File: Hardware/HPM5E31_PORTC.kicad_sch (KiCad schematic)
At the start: 1 part, among them U1 HPM5E31IGN1

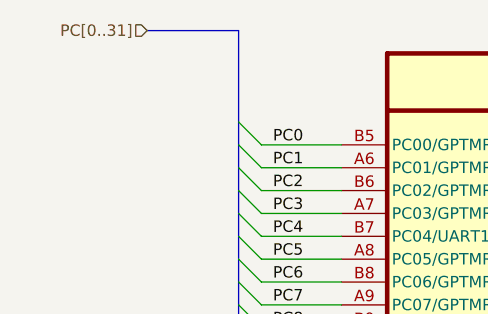
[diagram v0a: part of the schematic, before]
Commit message: 新增ESC IO引出，ESC CTR LED，EUI接口
编码器接口电源输出加保险，SPI加ESD
PY32ADC外部接口加ESD
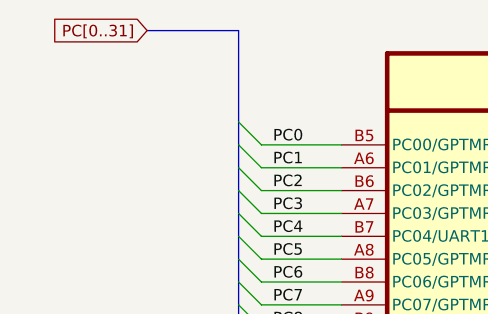
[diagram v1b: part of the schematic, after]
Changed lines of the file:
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@@
 		)
 	)
-	(hierarchical_label "PC[0..31]"
+	(global_label "PC[0..31]"
 		(shape input)
 		(at 40.64 41.91 180)
+		(fields_autoplaced yes)
 		(effects
 			(font
@@
 			(justify right)
 		)
+		(property "Intersheetrefs" "${INTERSHEET_REFS}"
+			(at 28.5833 41.91 0)
+			(effects
+				(font
+					(size 1.27 1.27)
+				)
+				(justify right)
+				(hide yes)
+			)
+		)
 	)

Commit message: 拉线
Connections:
- net PC0: no longer U1.B5 (PC00/GPTMR1.COMP0/UART0.TXD/MCAN0.TXD/ESC0.GPI63/ESC0.GPO00/PPI0.DQ24/XPI0.CB_CS0/PWM0.P0/TRGM.P00/ESC0.GPI15/OWR0.DAT)
- net PC1: no longer U1.A6 (PC01/GPTMR1.CAPT0/UART0.RXD/MCAN0.RXD/ESC0.GPI62/ESC0.GPO01/PPI0.DQ25/XPI0.CB_D1/PWM0.P1/TRGM.P01/ESC0.GPI14/OWR1.DAT)
- net PC10: no longer U1.D5 (PC10/GPTMR0.COMP2/UART2.DE/UART2.RTS/SPI1.SCLK/MCAN2.STBY/ESC0.GPI53/ESC0.GPO10/PPI0.DQ20/XPI0.CB_D0/PWM1.P2/TRGM.P10/ESC0.GPI05/QEI1.F/ESC0.CTR1)
- net PC11: no longer U1.C6 (PC11/UART2.CTS/SPI1.CS0/ESC0.GPI52/ESC0.GPO11/PPI0.DQ21/XPI0.CB_DQS/PWM1.P3/TRGM.P11/ESC0.GPI04/QEI1.H0/ESC0.CTR2)
- net PC12: no longer U1.D6 (PC12/UART3.CTS/I2C1.SDA/SPI1.MISO/ESC0.GPI51/ESC0.GPO12/PPI0.DM2/XPI0.CA_D2/PWM1.P4/TRGM.P12/ESC0.GPI03/QEI1.Z/QEO1.Z/ESC0.CTR3)
- net PC13: no longer U1.C7 (PC13/GPTMR1.COMP3/UART3.DE/UART3.RTS/I2C1.SCL/SPI1.MOSI/MCAN3.STBY/ESC0.GPI50/ESC0.GPO13/PPI0.DQ18/XPI0.CA_CS1/PWM1.P5/TRGM.P13/ESC0.GPI02/QEI1.A/QEO1.A/ESC0.CTR4)
- net PC14: no longer U1.D7 (PC14/UART3.RXD/SPI1.DAT2/MCAN3.RXD/ESC0.GPI49/ESC0.GPO14/PPI0.DQ19/PWM1.P6/TRGM.P14/ESC0.GPI01/QEI1.B/QEO1.B/ESC0.CTR5)
- net PC15: now also U1.J9 (VANA); no longer U1.C8 (PC15/GPTMR0.COMP3/UART3.TXD/SPI1.DAT3/MCAN3.TXD/ESC0.GPI48/ESC0.GPO15/PPI0.DM3/XPI0.CA_D0/PWM1.P7/TRGM.P15/ESC0.GPI00/ESC0.CTR6)
- net PC16: no longer U1.D8 (PC16/GPTMR3.COMP0/UART4.TXD/ESC0.GPI47/ESC0.GPO16/PPI0.DQ16/XPI0.CA_DQS/ESC0.CTR7)
- net PC17: no longer U1.C9 (PC17/GPTMR3.CAPT0/UART4.RXD/ESC0.GPI46/ESC0.GPO17/PPI0.DQ17/ESC0.CTR8)
- net PC18: now also U1.H8 (VSSA); no longer U1.A10 (PC18/GPTMR3.COMP1/UART4.DE/UART4.RTS/ESC0.GPI45/ESC0.GPO18/PPI0.DQ04/ESC0.CTR0)
- net PC19: no longer U1.B10 (PC19/GPTMR3.CAPT1/UART4.CTS/SPI2.CS3/ESC0.GPI44/ESC0.GPO19/PPI0.DQ05/ESC0.CTR1)
- net PC2: no longer U1.B6 (PC02/GPTMR1.COMP1/UART0.DE/UART0.RTS/I2C2.SCL/MCAN0.STBY/ESC0.GPI61/ESC0.GPO02/PPI0.DQ22/XPI0.CB_D2/PWM0.P2/TRGM.P02/ESC0.GPI13/QEI0.H1)
- net PC20: no longer U1.A11 (PC20/UART5.CTS/SPI3.SCLK/ESC0.GPI43/ESC0.GPO20/PPI0.DQ06/ESC0.CTR2)
- net PC21: no longer U1.B11 (PC21/GPTMR3.COMP2/UART5.DE/UART5.RTS/SPI3.CS0/ESC0.GPI42/ESC0.GPO21/PPI0.DQ07/ESC0.CTR3/QEO1.Z)
- net PC22: no longer U1.A12 (PC22/GPTMR2.CAPT0/UART5.RXD/SPI3.MISO/ESC0.GPI41/ESC0.GPO22/PPI0.CTR2/QEO1.B)
- net PC23: no longer U1.A13 (PC23/GPTMR2.COMP0/UART5.TXD/SPI3.MOSI/ESC0.GPI40/ESC0.GPO23/PPI0.DQ08/QEO1.A)
- net PC24: no longer U1.B14 (PC24/GPTMR2.COMP1/UART6.TXD/SPI2.CS2/ESC0.GPI39/ESC0.GPO24/PPI0.DQ09)
- net PC25: no longer U1.C14 (PC25/GPTMR2.CAPT1/UART6.RXD/SPI2.CS1/ESC0.GPI38/ESC0.GPO25/PPI0.DQ11)
- net PC26: no longer U1.D14 (PC26/GPTMR2.COMP2/UART6.DE/UART6.RTS/SPI2.SCLK/ESC0.GPI37/ESC0.GPO26/PPI0.DQ12/QEI1.H1)
- net PC27: no longer U1.D13 (PC27/UART6.CTS/SPI2.CS0/ESC0.GPI36/ESC0.GPO27/PPI0.CTR0/ESC0.CTR4/QEI1.F)
- net PC28: no longer U1.E14 (PC28/UART7.CTS/SPI2.MISO/ESC0.GPI35/ESC0.GPO28/PPI0.DM0/ESC0.CTR5/QEI1.H0)
- net PC29: no longer U1.E13 (PC29/GPTMR3.COMP3/UART7.DE/UART7.RTS/SPI2.MOSI/ESC0.GPI34/ESC0.GPO29/PPI0.CLK/ESC0.CTR6/QEI1.Z/SOC.REF0)
- net PC3: no longer U1.A7 (PC03/GPTMR1.CAPT1/UART0.CTS/I2C2.SDA/SPI1.CS3/MCAN1.STBY/ESC0.GPI60/ESC0.GPO03/PPI0.DQ26/XPI0.CB_D3/PWM0.P3/TRGM.P03/ESC0.GPI12/QEI0.F)
- net PC30: no longer U1.F14 (PC30/UART7.RXD/SPI2.DAT2/ESC0.GPI33/ESC0.GPO30/PPI0.CS0/ESC0.CTR7/QEI1.A/SOC.REF1)
- net PC31: no longer U1.F13 (PC31/GPTMR2.COMP3/UART7.TXD/SPI2.DAT3/ESC0.GPI32/ESC0.GPO31/PPI0.CS1/ESC0.CTR8/QEI1.B)
- net PC4: no longer U1.B7 (PC04/UART1.CTS/SPI0.SCLK/MCAN1.RXD/ESC0.GPI59/ESC0.GPO04/PPI0.DQ27/XPI0.CB_SCLK/PWM0.P4/TRGM.P04/ESC0.GPI11/QEI0.H0)
- net PC5: no longer U1.A8 (PC05/GPTMR1.COMP2/UART1.DE/UART1.RTS/SPI0.CS0/MCAN1.TXD/ESC0.GPI58/ESC0.GPO05/PPI0.DQ28/XPI0.CA_CS0/PWM0.P5/TRGM.P05/ESC0.GPI10/QEI0.Z/QEO0.Z)
- net PC6: no longer U1.B8 (PC06/GPTMR0.CAPT0/UART1.RXD/I2C3.SDA/SPI0.MISO/ESC0.GPI57/ESC0.GPO06/PPI0.DQ29/XPI0.CA_D1/PWM0.P6/TRGM.P06/ESC0.GPI09/QEI0.B/QEO0.B)
- net PC7: now also U1.N1 (DCDC_GND); no longer U1.A9 (PC07/GPTMR0.COMP0/UART1.TXD/I2C3.SCL/SPI0.MOSI/ESC0.GPI56/ESC0.GPO07/PPI0.DQ30/XPI0.CA_D3/PWM0.P7/TRGM.P07/ESC0.GPI08/QEI0.A/QEO0.A)
- net PC8: now also U1.P2 (DCDC_GND); no longer U1.B9 (PC08/GPTMR0.COMP1/UART2.TXD/I2C0.SCL/SPI1.CS2/MCAN2.TXD/ESC0.GPI55/ESC0.GPO08/PPI0.DQ31/XPI0.CA_SCLK/PWM1.P0/TRGM.P08/ESC0.GPI07)
- net PC9: no longer U1.C5 (PC09/GPTMR0.CAPT1/UART2.RXD/I2C0.SDA/SPI1.CS1/MCAN2.RXD/ESC0.GPI54/ESC0.GPO09/PPI0.DQ23/XPI0.CB_CS1/PWM1.P1/TRGM.P09/ESC0.GPI06/QEI1.H1/ESC0.CTR0)
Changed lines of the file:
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@@
+		)
+	)
+	(label "PC30"
+		(at 54.61 130.81 0)
+		(effects
+			(font
+				(size 1.27 1.27)
+			)
+			(justify left bottom)
+		)
+	)
+	(label "PC27"
+		(at 54.61 123.19 0)
+		(effects
+			(font
+				(size 1.27 1.27)
+			)
+			(justify left bottom)
+		)
+	)
+	(label "PC20"
+		(at 54.61 105.41 0)
+		(effects
+			(font
+				(size 1.27 1.27)
+			)
+			(justify left bottom)
+		)
+	)
+	(label "PC4"
+		(at 54.61 64.77 0)
+		(effects
+			(font
+				(size 1.27 1.27)
+			)
+			(justify left bottom)
+		)
+	)
+	(label "PC16"
+		(at 54.61 95.25 0)
+		(effects
+			(font
+				(size 1.27 1.27)
+			)
+			(justify left bottom)
+		)
+	)
+	(label "PC15"
+		(at 54.61 92.71 0)
+		(effects
+			(font
+				(size 1.27 1.27)
+			)
+			(justify left bottom)
+		)
+	)
+	(label "PC12"
+		(at 54.61 85.09 0)
+		(effects
+			(font
+				(size 1.27 1.27)
+			)
+			(justify left bottom)
+		)
+	)
+	(label "PC6"
+		(at 54.61 69.85 0)
+		(effects
+			(font
+				(size 1.27 1.27)
+			)
+			(justify left bottom)
+		)
+	)
+	(label "PC31"
+		(at 54.61 133.35 0)
+		(effects
+			(font
+				(size 1.27 1.27)
+			)
+			(justify left bottom)
+		)
+	)
+	(label "PC18"
+		(at 54.61 100.33 0)
+		(effects
+			(font
+				(size 1.27 1.27)
+			)
+			(justify left bottom)
+		)
+	)
+	(label "PC14"
+		(at 54.61 90.17 0)
+		(effects
+			(font
+				(size 1.27 1.27)
+			)
+			(justify left bottom)
+		)
+	)
+	(label "PC0"
+		(at 54.61 54.61 0)
+		(effects
+			(font
+				(size 1.27 1.27)
+			)
+			(justify left bottom)
+		)
+	)
+	(label "PC7"
+		(at 54.61 72.39 0)
+		(effects
+			(font
+				(size 1.27 1.27)
+			)
+			(justify left bottom)
+		)
+	)
+	(label "PC17"
+		(at 54.61 97.79 0)
+		(effects
+			(font
+				(size 1.27 1.27)
+			)
+			(justify left bottom)
+		)
+	)
+	(label "PC5"
+		(at 54.61 67.31 0)
+		(effects
+			(font
+				(size 1.27 1.27)
+			)
+			(justify left bottom)
+		)
+	)
+	(label "PC13"
+		(at 54.61 87.63 0)
+		(effects
+			(font
+				(size 1.27 1.27)
+			)
+			(justify left bottom)
+		)
+	)
+	(label "PC2"
+		(at 54.61 59.69 0)
+		(effects
+			(font
+				(size 1.27 1.27)
+			)
+			(justify left bottom)
+		)
+	)
+	(label "PC29"
+		(at 54.61 128.27 0)
+		(effects
+			(font
+				(size 1.27 1.27)
+			)
+			(justify left bottom)
+		)
+	)
+	(label "PC23"
+		(at 54.61 113.03 0)
+		(effects
+			(font
+				(size 1.27 1.27)
+			)
+			(justify left bottom)
 		)
 	)
 	(label "PC10"
 		(at 54.61 80.01 0)
-		(effects
-			(font
-				(size 1.27 1.27)
-			)
-			(justify left bottom)
-		)
-	)
-	(label "PC30"
-		(at 54.61 130.81 0)
-		(effects
-			(font
-				(size 1.27 1.27)
-			)
-			(justify left bottom)
-		)
-	)
-	(label "PC27"
-		(at 54.61 123.19 0)
-		(effects
-			(font
-				(size 1.27 1.27)
-			)
-			(justify left bottom)
-		)
-	)
-	(label "PC20"
-		(at 54.61 105.41 0)
-		(effects
-			(font
-				(size 1.27 1.27)
-			)
-			(justify left bottom)
-		)
-	)
-	(label "PC4"
-		(at 54.61 64.77 0)
-		(effects
-			(font
-				(size 1.27 1.27)
-			)
-			(justify left bottom)
-		)
-	)
-	(label "PC16"
-		(at 54.61 95.25 0)
-		(effects
-			(font
-				(size 1.27 1.27)
-			)
-			(justify left bottom)
-		)
-	)
-	(label "PC15"
-		(at 54.61 92.71 0)
-		(effects
-			(font
-				(size 1.27 1.27)
-			)
-			(justify left bottom)
-		)
-	)
-	(label "PC12"
-		(at 54.61 85.09 0)
-		(effects
-			(font
-				(size 1.27 1.27)
-			)
-			(justify left bottom)
-		)
-	)
-	(label "PC6"
-		(at 54.61 69.85 0)
-		(effects
-			(font
-				(size 1.27 1.27)
-			)
-			(justify left bottom)
-		)
-	)
-	(label "PC31"
-		(at 54.61 133.35 0)
-		(effects
-			(font
-				(size 1.27 1.27)
-			)
-			(justify left bottom)
-		)
-	)
-	(label "PC18"
-		(at 54.61 100.33 0)
-		(effects
-			(font
-				(size 1.27 1.27)
-			)
-			(justify left bottom)
-		)
-	)
-	(label "PC14"
-		(at 54.61 90.17 0)
-		(effects
-			(font
-				(size 1.27 1.27)
-			)
-			(justify left bottom)
-		)
-	)
-	(label "PC0"
-		(at 54.61 54.61 0)
-		(effects
-			(font
-				(size 1.27 1.27)
-			)
-			(justify left bottom)
-		)
-	)
-	(label "PC7"
-		(at 54.61 72.39 0)
-		(effects
-			(font
-				(size 1.27 1.27)
-			)
-			(justify left bottom)
-		)
-	)
-	(label "PC17"
-		(at 54.61 97.79 0)
-		(effects
-			(font
-				(size 1.27 1.27)
-			)
-			(justify left bottom)
-		)
-	)
-	(label "PC5"
-		(at 54.61 67.31 0)
-		(effects
-			(font
-				(size 1.27 1.27)
-			)
-			(justify left bottom)
-		)
-	)
-	(label "PC13"
-		(at 54.61 87.63 0)
-		(effects
-			(font
-				(size 1.27 1.27)
-			)
-			(justify left bottom)
-		)
-	)
-	(label "PC2"
-		(at 54.61 59.69 0)
-		(effects
-			(font
-				(size 1.27 1.27)
-			)
-			(justify left bottom)
-		)
-	)
-	(label "PC29"
-		(at 54.61 128.27 0)
-		(effects
-			(font
-				(size 1.27 1.27)
-			)
-			(justify left bottom)
-		)
-	)
-	(label "PC23"
-		(at 54.61 113.03 0)
 		(effects
 			(font
@@
 		(lib_id "HPM5E00_Library:HPM5E31IGN1")
 		(at 67.31 44.45 0)
-		(unit 6)
+		(unit 1)
 		(exclude_from_sim no)
 		(in_bom yes)
@@
 		(pin "L6"
 		)
-		(instances
-			(project "HPM5E31_ECatDualFOC"
-				(path "/a07e9810-3899-4327-ba8f-f24142a7c70e/b9a8d5a3-7d25-4818-87f6-adc719379948/8f1a015a-67d3-4afd-9e89-f3485933260a"
-					(reference "U1")
-					(unit 6)
-				)
-			)
-		)
-	)
+	)

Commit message: 修存档拉线
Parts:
- renumbered U1 to U3
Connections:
- net PC0: now also U3.B5 (PC00/GPTMR1.COMP0/UART0.TXD/MCAN0.TXD/ESC0.GPI63/ESC0.GPO00/PPI0.DQ24/XPI0.CB_CS0/PWM0.P0/TRGM.P00/ESC0.GPI15/OWR0.DAT)
- net PC1: now also U3.A6 (PC01/GPTMR1.CAPT0/UART0.RXD/MCAN0.RXD/ESC0.GPI62/ESC0.GPO01/PPI0.DQ25/XPI0.CB_D1/PWM0.P1/TRGM.P01/ESC0.GPI14/OWR1.DAT)
- net PC10: now also U3.D5 (PC10/GPTMR0.COMP2/UART2.DE/UART2.RTS/SPI1.SCLK/MCAN2.STBY/ESC0.GPI53/ESC0.GPO10/PPI0.DQ20/XPI0.CB_D0/PWM1.P2/TRGM.P10/ESC0.GPI05/QEI1.F/ESC0.CTR1)
- net PC11: now also U3.C6 (PC11/UART2.CTS/SPI1.CS0/ESC0.GPI52/ESC0.GPO11/PPI0.DQ21/XPI0.CB_DQS/PWM1.P3/TRGM.P11/ESC0.GPI04/QEI1.H0/ESC0.CTR2)
- net PC12: now also U3.D6 (PC12/UART3.CTS/I2C1.SDA/SPI1.MISO/ESC0.GPI51/ESC0.GPO12/PPI0.DM2/XPI0.CA_D2/PWM1.P4/TRGM.P12/ESC0.GPI03/QEI1.Z/QEO1.Z/ESC0.CTR3)
- net PC13: now also U3.C7 (PC13/GPTMR1.COMP3/UART3.DE/UART3.RTS/I2C1.SCL/SPI1.MOSI/MCAN3.STBY/ESC0.GPI50/ESC0.GPO13/PPI0.DQ18/XPI0.CA_CS1/PWM1.P5/TRGM.P13/ESC0.GPI02/QEI1.A/QEO1.A/ESC0.CTR4)
- net PC14: now also U3.D7 (PC14/UART3.RXD/SPI1.DAT2/MCAN3.RXD/ESC0.GPI49/ESC0.GPO14/PPI0.DQ19/PWM1.P6/TRGM.P14/ESC0.GPI01/QEI1.B/QEO1.B/ESC0.CTR5)
- net PC15: now also U3.C8 (PC15/GPTMR0.COMP3/UART3.TXD/SPI1.DAT3/MCAN3.TXD/ESC0.GPI48/ESC0.GPO15/PPI0.DM3/XPI0.CA_D0/PWM1.P7/TRGM.P15/ESC0.GPI00/ESC0.CTR6); no longer U3.J9 (VANA)
- net PC16: now also U3.D8 (PC16/GPTMR3.COMP0/UART4.TXD/ESC0.GPI47/ESC0.GPO16/PPI0.DQ16/XPI0.CA_DQS/ESC0.CTR7)
- net PC17: now also U3.C9 (PC17/GPTMR3.CAPT0/UART4.RXD/ESC0.GPI46/ESC0.GPO17/PPI0.DQ17/ESC0.CTR8)
- net PC18: now also U3.A10 (PC18/GPTMR3.COMP1/UART4.DE/UART4.RTS/ESC0.GPI45/ESC0.GPO18/PPI0.DQ04/ESC0.CTR0); no longer U3.H8 (VSSA)
- net PC19: now also U3.B10 (PC19/GPTMR3.CAPT1/UART4.CTS/SPI2.CS3/ESC0.GPI44/ESC0.GPO19/PPI0.DQ05/ESC0.CTR1)
- net PC2: now also U3.B6 (PC02/GPTMR1.COMP1/UART0.DE/UART0.RTS/I2C2.SCL/MCAN0.STBY/ESC0.GPI61/ESC0.GPO02/PPI0.DQ22/XPI0.CB_D2/PWM0.P2/TRGM.P02/ESC0.GPI13/QEI0.H1)
- net PC20: now also U3.A11 (PC20/UART5.CTS/SPI3.SCLK/ESC0.GPI43/ESC0.GPO20/PPI0.DQ06/ESC0.CTR2)
- net PC21: now also U3.B11 (PC21/GPTMR3.COMP2/UART5.DE/UART5.RTS/SPI3.CS0/ESC0.GPI42/ESC0.GPO21/PPI0.DQ07/ESC0.CTR3/QEO1.Z)
- net PC22: now also U3.A12 (PC22/GPTMR2.CAPT0/UART5.RXD/SPI3.MISO/ESC0.GPI41/ESC0.GPO22/PPI0.CTR2/QEO1.B)
- net PC23: now also U3.A13 (PC23/GPTMR2.COMP0/UART5.TXD/SPI3.MOSI/ESC0.GPI40/ESC0.GPO23/PPI0.DQ08/QEO1.A)
- net PC24: now also U3.B14 (PC24/GPTMR2.COMP1/UART6.TXD/SPI2.CS2/ESC0.GPI39/ESC0.GPO24/PPI0.DQ09)
- net PC25: now also U3.C14 (PC25/GPTMR2.CAPT1/UART6.RXD/SPI2.CS1/ESC0.GPI38/ESC0.GPO25/PPI0.DQ11)
- net PC26: now also U3.D14 (PC26/GPTMR2.COMP2/UART6.DE/UART6.RTS/SPI2.SCLK/ESC0.GPI37/ESC0.GPO26/PPI0.DQ12/QEI1.H1)
- net PC27: now also U3.D13 (PC27/UART6.CTS/SPI2.CS0/ESC0.GPI36/ESC0.GPO27/PPI0.CTR0/ESC0.CTR4/QEI1.F)
- net PC28: now also U3.E14 (PC28/UART7.CTS/SPI2.MISO/ESC0.GPI35/ESC0.GPO28/PPI0.DM0/ESC0.CTR5/QEI1.H0)
- net PC29: now also U3.E13 (PC29/GPTMR3.COMP3/UART7.DE/UART7.RTS/SPI2.MOSI/ESC0.GPI34/ESC0.GPO29/PPI0.CLK/ESC0.CTR6/QEI1.Z/SOC.REF0)
- net PC3: now also U3.A7 (PC03/GPTMR1.CAPT1/UART0.CTS/I2C2.SDA/SPI1.CS3/MCAN1.STBY/ESC0.GPI60/ESC0.GPO03/PPI0.DQ26/XPI0.CB_D3/PWM0.P3/TRGM.P03/ESC0.GPI12/QEI0.F)
- net PC30: now also U3.F14 (PC30/UART7.RXD/SPI2.DAT2/ESC0.GPI33/ESC0.GPO30/PPI0.CS0/ESC0.CTR7/QEI1.A/SOC.REF1)
- net PC31: now also U3.F13 (PC31/GPTMR2.COMP3/UART7.TXD/SPI2.DAT3/ESC0.GPI32/ESC0.GPO31/PPI0.CS1/ESC0.CTR8/QEI1.B)
- net PC4: now also U3.B7 (PC04/UART1.CTS/SPI0.SCLK/MCAN1.RXD/ESC0.GPI59/ESC0.GPO04/PPI0.DQ27/XPI0.CB_SCLK/PWM0.P4/TRGM.P04/ESC0.GPI11/QEI0.H0)
- net PC5: now also U3.A8 (PC05/GPTMR1.COMP2/UART1.DE/UART1.RTS/SPI0.CS0/MCAN1.TXD/ESC0.GPI58/ESC0.GPO05/PPI0.DQ28/XPI0.CA_CS0/PWM0.P5/TRGM.P05/ESC0.GPI10/QEI0.Z/QEO0.Z)
- net PC6: now also U3.B8 (PC06/GPTMR0.CAPT0/UART1.RXD/I2C3.SDA/SPI0.MISO/ESC0.GPI57/ESC0.GPO06/PPI0.DQ29/XPI0.CA_D1/PWM0.P6/TRGM.P06/ESC0.GPI09/QEI0.B/QEO0.B)
- net PC7: now also U3.A9 (PC07/GPTMR0.COMP0/UART1.TXD/I2C3.SCL/SPI0.MOSI/ESC0.GPI56/ESC0.GPO07/PPI0.DQ30/XPI0.CA_D3/PWM0.P7/TRGM.P07/ESC0.GPI08/QEI0.A/QEO0.A); no longer U3.N1 (DCDC_GND)
- net PC8: now also U3.B9 (PC08/GPTMR0.COMP1/UART2.TXD/I2C0.SCL/SPI1.CS2/MCAN2.TXD/ESC0.GPI55/ESC0.GPO08/PPI0.DQ31/XPI0.CA_SCLK/PWM1.P0/TRGM.P08/ESC0.GPI07); no longer U3.P2 (DCDC_GND)
- net PC9: now also U3.C5 (PC09/GPTMR0.CAPT1/UART2.RXD/I2C0.SDA/SPI1.CS1/MCAN2.RXD/ESC0.GPI54/ESC0.GPO09/PPI0.DQ23/XPI0.CB_CS1/PWM1.P1/TRGM.P09/ESC0.GPI06/QEI1.H1/ESC0.CTR0)
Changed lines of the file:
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@@
 		(lib_id "HPM5E00_Library:HPM5E31IGN1")
 		(at 67.31 44.45 0)
-		(unit 1)
+		(unit 6)
 		(exclude_from_sim no)
 		(in_bom yes)
@@
 		(dnp no)
 		(fields_autoplaced yes)
-		(property "Reference" "U1"
+		(property "Reference" "U3"
 			(at 256.54 90.1699 0)
 			(effects
@@
 		(pin "L6"
 		)
+		(instances
+			(project "HPM5E31_ECatDualFOC"
+				(path "/a07e9810-3899-4327-ba8f-f24142a7c70e/b9a8d5a3-7d25-4818-87f6-adc719379948/8f1a015a-67d3-4afd-9e89-f3485933260a"
+					(reference "U3")
+					(unit 6)
+				)
+			)
+		)
 	)
